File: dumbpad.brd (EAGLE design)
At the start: 97 x 78.5 mm, 42 parts

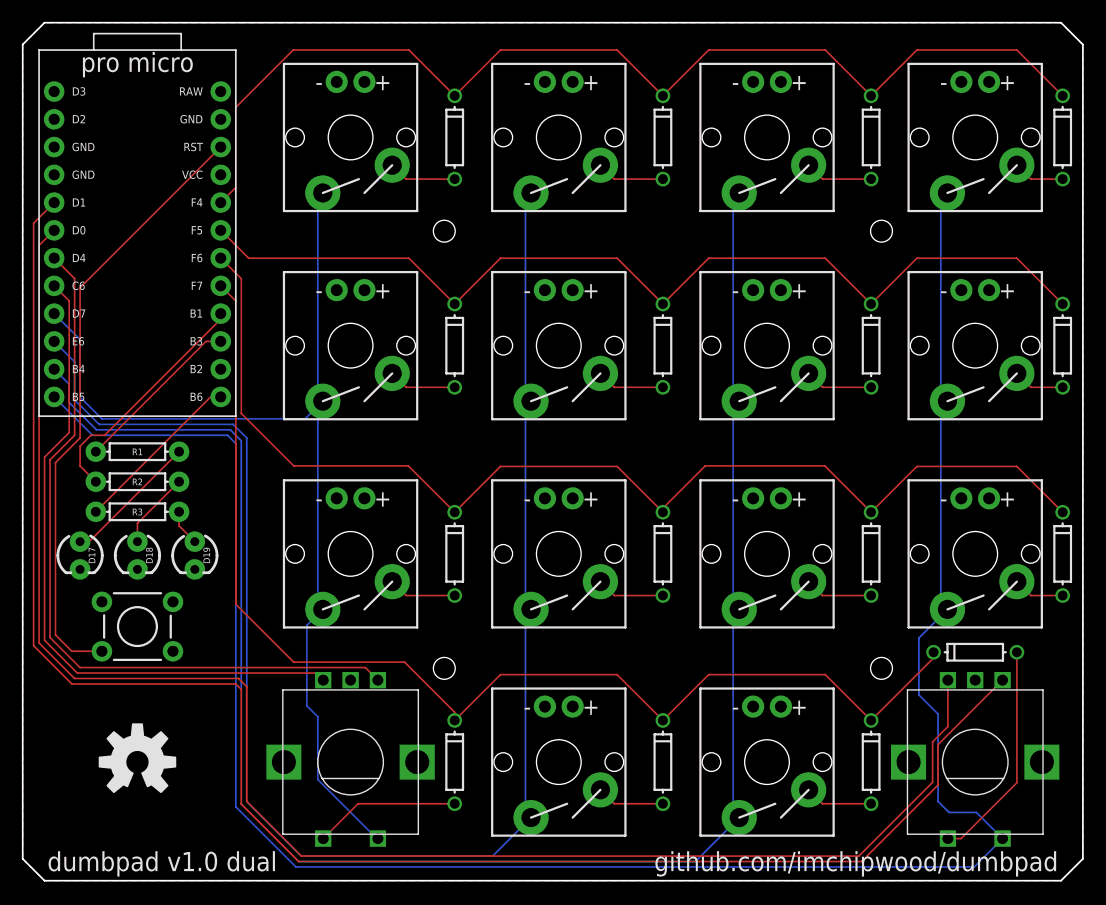
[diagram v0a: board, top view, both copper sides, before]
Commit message: dualencoder now has cherry/encoder sockets for putting encoders on either top row or bottom row
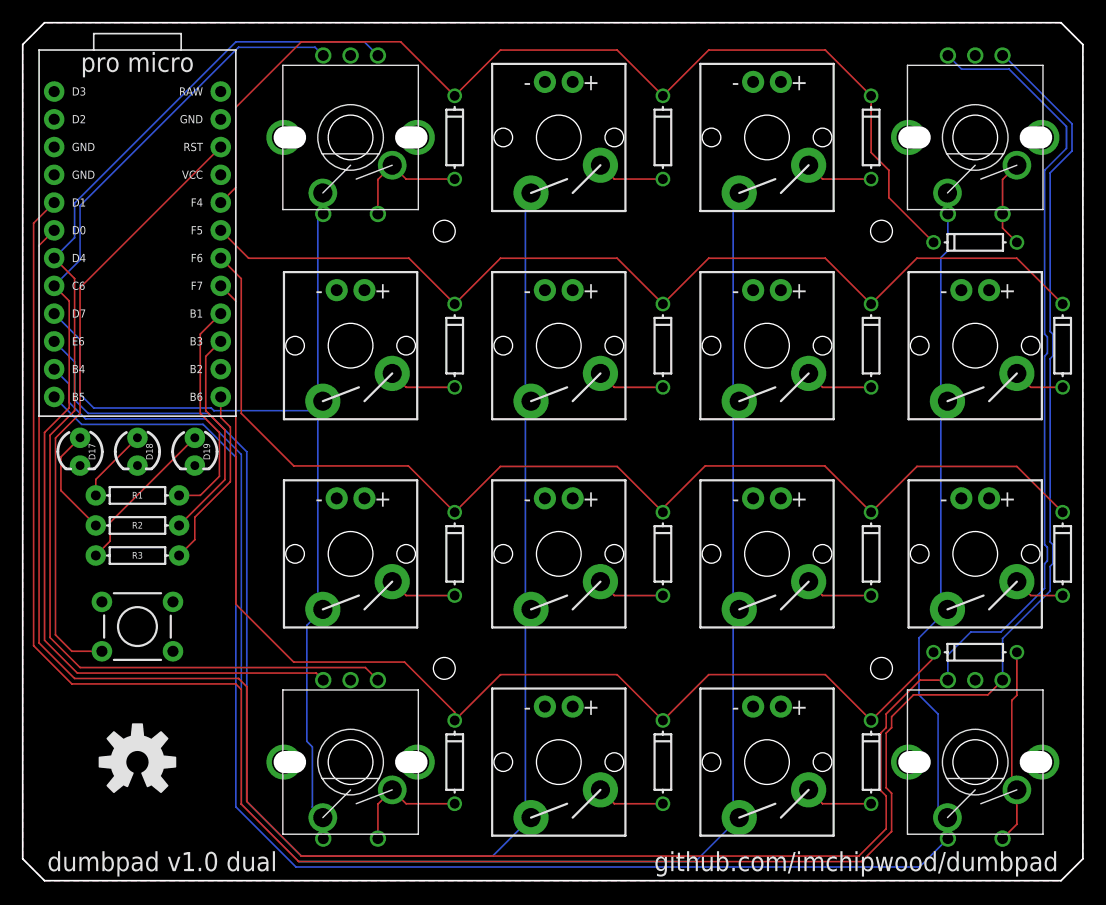
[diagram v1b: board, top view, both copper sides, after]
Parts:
- removed S1, S4: MOMENTARY-SWITCH-SPST-LED-PTH-CHERRY, SparkFun-Switches:CHERRY-MX-LED
- added U$1, U$2: CHERRY-MX-ENCODER, cpwood:CHERRY-MX-ENCODER
- RE0, RE1: value EC12E_SW -> CHERRY-MX-ENCODER; device switch-alps:ALPS_EC12E_SW -> cpwood:CHERRY-MX-ENCODER
- moved D4 12.5 mm to (87.2, 58.4), turned to 180 degrees
- moved D17 9.50 mm to (5.25, 39.2)
- moved D18 9.50 mm to (10.5, 39.2)
- moved D19 9.50 mm to (15.8, 39.2)
- moved R1 4.00 mm to (10.5, 35.2), turned to 0 degrees
- moved R2 4.00 mm to (10.5, 32.5), turned to 0 degrees
- moved R3 4.00 mm to (10.5, 29.8), turned to 0 degrees
- turned RE0 to 0 degrees
- turned RE1 to 0 degrees
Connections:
- net COL0: now also RE0.E, RE0.S1_1, U$1.E, U$1.S1_1; no longer RE0.D, S1.S2
- net COL3: now also RE1.E, RE1.S1_1, U$2.E, U$2.S1_1; no longer RE1.D, S4.S2
- net ENCODER0_L0: now also U$1.B
- net ENCODER0_L1: now also U$1.A
- net ENCODER1_L0: now also U$2.A
- net ENCODER1_L1: now also U$2.B
- net GND: now also U$1.C, U$2.C
- net LED0: now also R2.P$2; no longer R1.P$2
- net LED1: now also R1.P$2; no longer R2.P$2
- net N$1: now also U$2.D, U$2.S2_1; no longer S4.S1
- net N$10: now also R1.P$1; no longer R2.P$1
- net N$11: now also RE1.D, RE1.S2_1; no longer RE1.E
- net N$14: now also RE0.D, RE0.S2_1; no longer RE0.E
- net N$4: now also U$1.D, U$1.S2_1; no longer S1.S1
- net N$5: now also R2.P$1; no longer R1.P$1
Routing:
- net ENCODER1_L1: track 147.0 -> 219.6 mm
- net ENCODER1_L0: track 153.3 -> 220.6 mm
- net ENCODER0_L1: track 68.0 -> 108.2 mm
- net ENCODER0_L0: track 60.9 -> 97.8 mm
- net N$15: track 3.33 -> 14.5 mm
- net COL3: track 190.9 -> 181.7 mm
- net N$4: track 6.24 -> 11.2 mm
- net ROW0: track 99.3 -> 94.7 mm
- net LED0: track 15.6 -> 19.9 mm
- net N$1: track 4.72 -> 8.15 mm
- net COL0: track 94.9 -> 92.0 mm
- net N$5: track 12.5 -> 10.1 mm
- net N$11: track 20.4 -> 18.0 mm
- net N$14: track 13.3 -> 11.2 mm
- net LED1: track 22.0 -> 20.8 mm
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
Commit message: dual + single encoder configuration
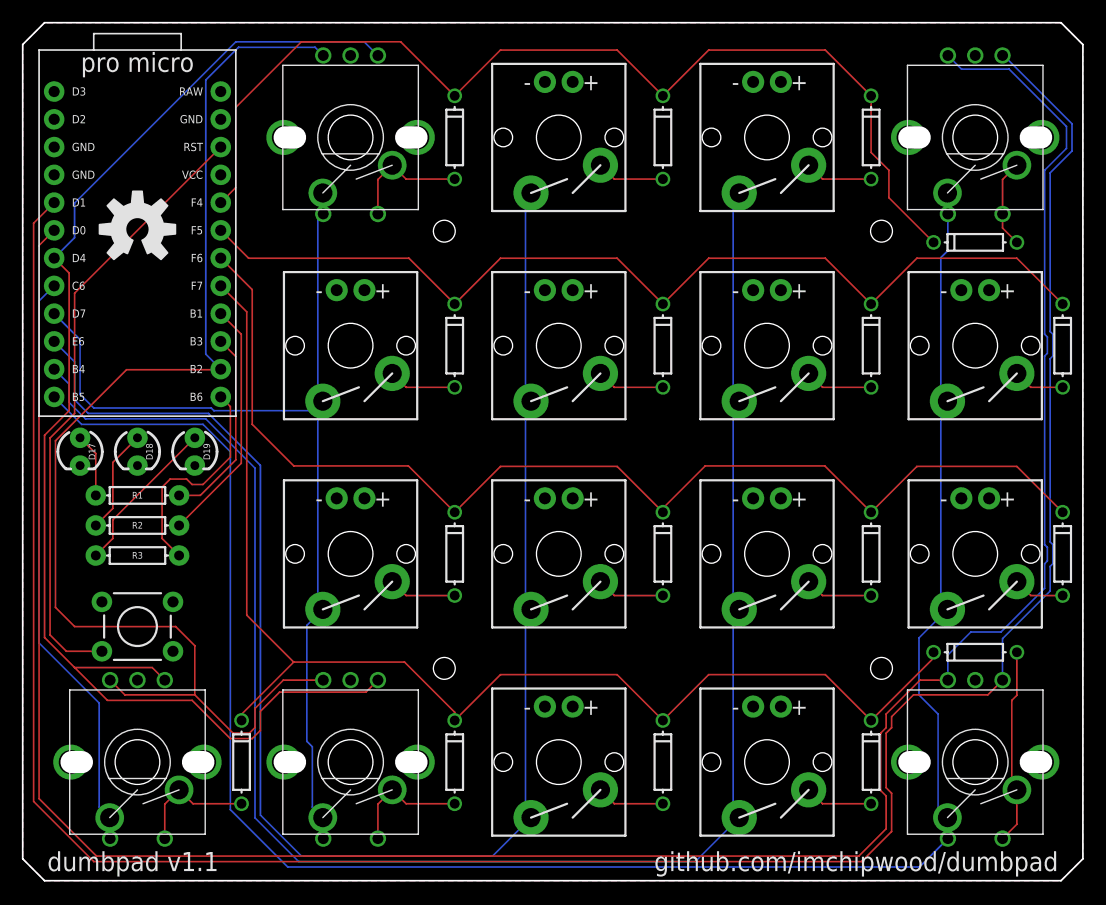
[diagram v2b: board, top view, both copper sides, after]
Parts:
- added D20: (no value), adafruit:DO-1N4148
- added RE_3_0: CHERRY-MX-ENCODER, cpwood:CHERRY-MX-ENCODER
- moved LOGO1 48.8 mm to (10.5, 59.6)
- moved LOGO2 48.8 mm to (10.5, 59.6)
- renumbered RE0 to RE_3_1, RE1 to RE_3_4, U$1 to RE_0_1, U$2 to RE_0_4
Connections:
- removed net NC/MOSI/B2: B1.14
- new net COL4: B1.12, RE_0_4.E, RE_0_4.S1_1, RE_3_4.E, RE_3_4.S1_1, S12.S2, S8.S2
- new net N$20: D20.A, RE_3_0.D, RE_3_0.S2_1
- net COL0: now also B1.8, RE_3_0.E, RE_3_0.S1_1; no longer B1.9, RE_0_1.E, RE_0_1.S1_1, RE_3_1.E, RE_3_1.S1_1, S5.S2, S9.S2
- net COL1: now also B1.9, RE_0_1.E, RE_0_1.S1_1, RE_3_1.E, RE_3_1.S1_1, S5.S2, S9.S2; no longer B1.10, S10.S2, S14.S2, S2.S2, S6.S2
- net COL2: now also B1.10, S10.S2, S14.S2, S2.S2, S6.S2; no longer B1.11, S11.S2, S15.S2, S3.S2, S7.S2
- net COL3: now also B1.11, S11.S2, S15.S2, S3.S2, S7.S2; no longer B1.12, RE_0_4.E, RE_0_4.S1_1, RE_3_4.E, RE_3_4.S1_1, S12.S2, S8.S2
- net ENCODER0_L0: now also B1.14, RE_3_0.B; no longer B1.8
- net ENCODER0_L1: now also RE_3_0.A
- net GND: now also RE_3_0.C
- net LED0: now also R1.P$2; no longer R2.P$2
- net LED1: now also R2.P$2; no longer R1.P$2
- net N$10: now also R2.P$1; no longer R1.P$1
- net N$5: now also R1.P$1; no longer R2.P$1
- net ROW3: now also D20.C
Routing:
- net COL4: track 0.00 -> 182.1 mm
- net COL1: track 143.8 -> 92.0 mm
- net COL0: track 92.0 -> 53.8 mm
- net COL3: track 181.7 -> 161.3 mm
- net ENCODER0_L0: track 97.8 -> 115.6 mm
- net COL2: track 161.3 -> 143.8 mm
- net ENCODER0_L1: track 108.2 -> 122.7 mm
- net N$20: track 0.00 -> 11.2 mm
- net ROW3: track 108.2 -> 115.5 mm
- net N$5: track 10.1 -> 5.87 mm
- net LED2: track 16.8 -> 20.6 mm
- net N$10: track 6.85 -> 9.60 mm
- net ENCODER1_L1: track 219.6 -> 221.8 mm
- net ENCODER1_L0: track 220.6 -> 222.8 mm
- net LED0: track 19.9 -> 17.9 mm
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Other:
- board text added: "dumbpad v1.1"
- board text removed: "dumbpad v1.0 dual"

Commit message: updating board and adding cam file
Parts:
- moved R1 1.00 mm to (10.5, 34.2)
- moved R2 1.00 mm to (10.5, 31.5)
- moved R3 1.00 mm to (10.5, 28.8)
- moved D17 0.50 mm to (5.25, 38.8)
- moved D18 0.50 mm to (10.5, 38.8)
- moved D19 0.50 mm to (15.8, 38.8)
- moved D20 0.50 mm to (19.5, 10.8)
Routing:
- net ENCODER1_L0: track 222.8 -> 218.4 mm
- net ENCODER1_L1: track 221.8 -> 219.9 mm
- net LED1: track 22.5 -> 23.5 mm
- net LED0: track 17.9 -> 18.9 mm
- net LED2: track 20.6 -> 21.2 mm
- net COL4: track 182.1 -> 181.6 mm
- net N$5: track 5.87 -> 6.37 mm
- net N$20: track 11.2 -> 10.7 mm
- net N$15: track 14.5 -> 15.0 mm
- net N$10: track 9.60 -> 10.1 mm

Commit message: minor changes
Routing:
- net ENCODER0_L0: track 115.6 -> 116.5 mm
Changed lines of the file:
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@@
 <wire x1="15.75" y1="17" x2="9.35" y2="17" width="0.1524" layer="1"/>
 <wire x1="15.75" y1="17" x2="15.75" y2="21.5" width="0.1524" layer="1"/>
-<wire x1="15.75" y1="21.5" x2="14" y2="23.25" width="0.1524" layer="1"/>
-<wire x1="14" y1="23.25" x2="4.75" y2="23.25" width="0.1524" layer="1"/>
-<wire x1="4.75" y1="23.25" x2="3" y2="25" width="0.1524" layer="1"/>
-<wire x1="3" y1="25" x2="3" y2="40.25" width="0.1524" layer="1"/>
+<wire x1="15.75" y1="21.5" x2="14.25" y2="23" width="0.1524" layer="1"/>
+<wire x1="14.25" y1="23" x2="3.5" y2="23" width="0.1524" layer="1"/>
+<wire x1="3.5" y1="23" x2="3" y2="23.5" width="0.1524" layer="1"/>
+<wire x1="3" y1="23.5" x2="3" y2="40.25" width="0.1524" layer="1"/>
 <wire x1="3" y1="40.25" x2="9.5" y2="46.75" width="0.1524" layer="1"/>
 <wire x1="18.07" y1="46.75" x2="18.12" y2="46.8" width="0.1524" layer="1"/>
@@
 <wire x1="8" y1="3.85" x2="7.96" y2="3.89" width="0.1524" layer="16"/>
 <wire x1="7.96" y1="3.89" x2="7.96" y2="5.77" width="0.1524" layer="16"/>
-<wire x1="7.96" y1="5.77" x2="7" y2="6.73" width="0.1524" layer="16"/>
+<wire x1="7.96" y1="5.77" x2="7.75" y2="5.98" width="0.1524" layer="16"/>
 <wire x1="1.5" y1="53.04" x2="2.88" y2="54.42" width="0.1524" layer="16"/>
-<wire x1="7" y1="6.73" x2="7" y2="16.5" width="0.1524" layer="16"/>
-<wire x1="7" y1="16.5" x2="1.5" y2="22" width="0.1524" layer="16"/>
+<wire x1="7.75" y1="5.98" x2="7.75" y2="15.75" width="0.1524" layer="16"/>
+<wire x1="7.75" y1="15.75" x2="1.5" y2="22" width="0.1524" layer="16"/>
 <wire x1="1.5" y1="22" x2="1.5" y2="53.04" width="0.1524" layer="16"/>
 </signal>
